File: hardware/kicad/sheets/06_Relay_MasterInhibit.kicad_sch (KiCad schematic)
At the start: 0 parts

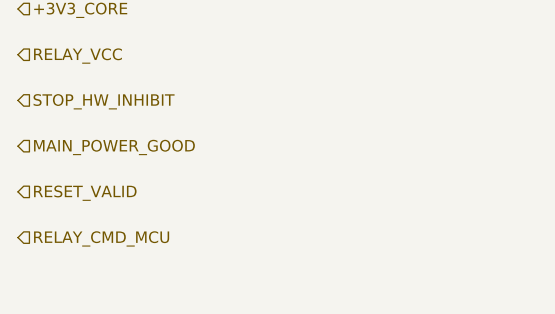
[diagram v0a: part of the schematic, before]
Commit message: Resolve independent watchdog service interface
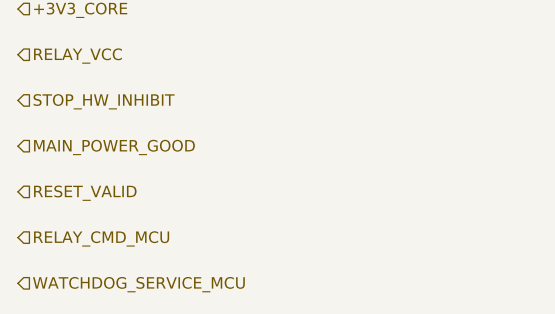
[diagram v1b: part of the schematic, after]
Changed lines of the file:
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@@
+    (effects (font (size 1.27 1.27)) (justify left))
+  )
+  (hierarchical_label "WATCHDOG_SERVICE_MCU" (shape input) (at 25.4 75.48 0)
     (effects (font (size 1.27 1.27)) (justify left))
   )

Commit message: Implement Package 07R safety output control
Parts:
- added C1: Timing capacitor — value set from selected watchd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, symbol IPC100:C
- added D1: Schottky + 12 V / 500 mW zener series flyback cla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, symbol IPC100:FLYBACK_CLAMP
- added K1: Omron G5Q-1 DC5-class, 5 V / 80 mA provisional, symbol IPC100:RELAY_SPDT
- added Q1: 2N7002P-class, 60 V logic N-MOSFET, symbol IPC100:NMOS
- added R1: 100 kΩ WDI fail-low / open-route bias, symbol IPC100:R
- added R10: 100 kΩ MASTER_INHIBIT fail-high, symbol IPC100:R
- added R2: 100 Ω gate resistor, symbol IPC100:R
- added R3: 100 kΩ MOSFET gate default-OFF bias, symbol IPC100:R
- added R4: 100 kΩ MAIN_POWER_GOOD fail-low, symbol IPC100:R
- added R5: 100 kΩ RESET_VALID fail-low, symbol IPC100:R
- added R6: 100 kΩ STOP_HW_INHIBIT fail-high, symbol IPC100:R
- added R7: 100 kΩ RELAY_CMD_MCU fail-low, symbol IPC100:R
- added R8: 100 kΩ WATCHDOG_VALID fail-low, symbol IPC100:R
- added R9: 100 kΩ ACTUATOR_PERMIT fail-low, symbol IPC100:R
- added U1: Independent window watchdog + 2-edge qualifier/la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, symbol IPC100:WINDOW_WATCHDOG
- added U2: Fail-safe four-condition authorization logic, symbol IPC100:AUTH4
- added U3: RELAY_CMD_MCU AND ACTUATOR_PERMIT, symbol IPC100:AND2
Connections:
- net +3V3_CORE: now also R10.2, R6.2, U1.5 (GND), U2.6 (GND), U3.3 (GND)
- net ACTUATOR_PERMIT: now also R9.2, U2.8 (INHIBIT), U3.1 (A)
- net MAIN_POWER_GOOD: now also R4.2, U1.2 (WDI), U2.5 (WD_VALID)
- net MASTER_INHIBIT: now also R10.1, U2.7 (PERMIT)
- net RELAY_CMD_MCU: now also R7.2, U3.2 (B)
- net RELAY_COM: now also K1.4 (COM)
- net RELAY_NC: now also K1.5 (NO)
- net RELAY_NO: now also K1.3 (NC)
- net RELAY_VCC: now also D1.2 (COIL_HIGH), K1.2 (COIL-)
- net RESET_VALID: now also R5.2, U1.3 (RESET_VALID), U2.3 (STOP_INHIBIT)
- net STOP_HW_INHIBIT: now also R6.1, U2.4 (RESET_VALID)
- net WATCHDOG_SERVICE_MCU: now also R1.2, U1.4 (MAIN_POWER_GOOD)
- net WATCHDOG_VALID: now also R8.2, U1.7 (TIMING), U2.2 (MAIN_GOOD)
- new net GND: C1.1, Q1.2 (D), R1.1, R3.1, R4.1, R5.1, R7.1, R8.1, R9.1, U1.1 (VDD), U2.1 (VDD), U3.5 (VDD)
- new net RELAY_COIL_LOW: D1.1 (COIL_LOW), K1.1 (COIL+), Q1.3 (S)
- new net RELAY_GATE: Q1.1 (G), R2.1, R3.2
- new net RELAY_GATE_AUTH: R2.2, U3.4 (Y)
- new net WATCHDOG_TIMING: C1.2, U1.6 (WATCHDOG_VALID)
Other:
- note added: "1 — INDEPENDENT WINDOW WATCHDOG / STARTUP QUALIFIER"
- note added: "2 — HARDWARE AUTHORIZATION (NO FIRMWARE BYPASS)"
- note added: "3 — RELAY REQUEST GATE, LOW-SIDE DRIVER & FLYBACK CLAMP"
- note added: "4 — HIERARCHICAL FUNCTIONAL INTERFACES"
- note added: "Deterministic local biases: open hierarchy, reset, partial power, or absent producer always resolves to the deauthorized state."
- note added: "No connectors, footprints, motor drivers, H-bridges, or PCB objects. RELAY_CMD_MCU remains generic; no THROWER_TRIGGER or additional motor/driver enables."
- note added: "PERMIT = MAIN_POWER_GOOD AND NOT STOP_HW_INHIBIT AND RESET_VALID AND WATCHDOG_VALID; MASTER_INHIBIT = NOT PERMIT"
- note added: "WDI transitions: 75 ms nominal, 40–100 ms valid. Static high/low invalid. Two valid edges plus RESET_VALID and MAIN_POWER_GOOD required. Timing fault latches invalid until reset/power cycle; loss response ≤250 ms."
- note removed: "Detailed implementation intentionally deferred to subsequent engineering package."
- note removed: "PACKAGE 01 PLACEHOLDER — NO CIRCUITRY OR FOOTPRINTS"
- title: IPC-100 Rev A — 06 Relay + Master Inhibit -> IPC-100 Rev A — 06 Safety Authorization, Independent Watchdog & Output Control

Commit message: Normalize Rev A reference designators
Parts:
- renumbered C1 to C601, D1 to D601, K1 to K601, Q1 to Q601, R1 to R601, R2 to R602, R3 to R603, R4 to R604, R5 to R605, R6 to R606, R7 to R607, R8 to R608, R9 to R609, R10 to R610, U1 to U601, U2 to U602, U3 to U603
